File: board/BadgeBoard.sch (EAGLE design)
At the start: 63 parts

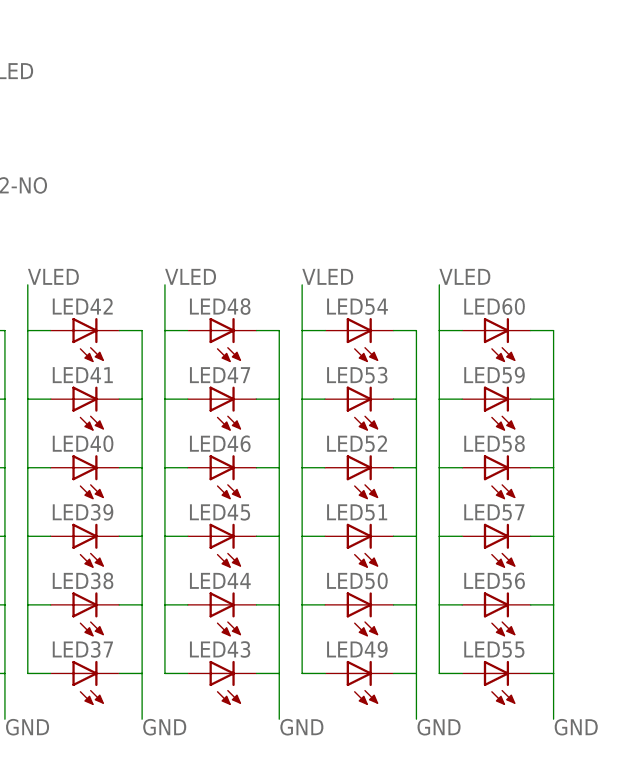
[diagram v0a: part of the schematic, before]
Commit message: add battery, redo layout a little
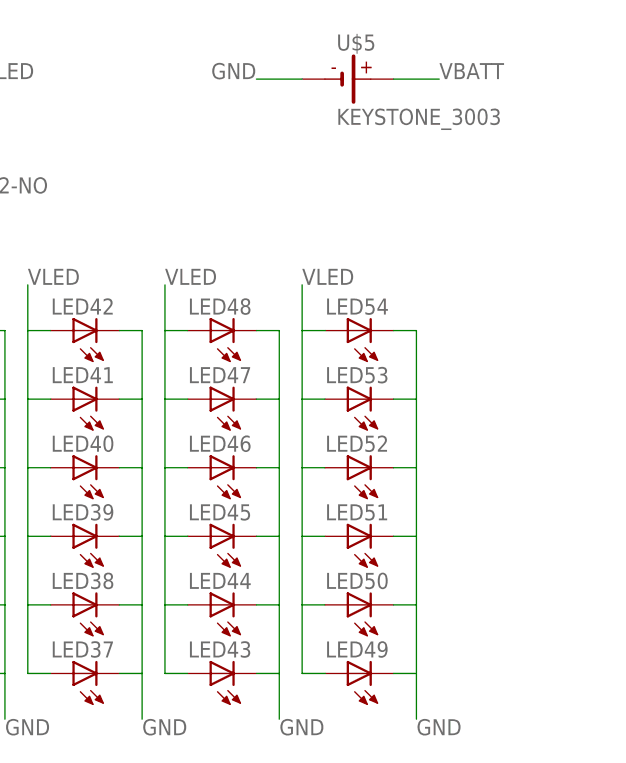
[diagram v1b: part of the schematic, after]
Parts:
- removed LED55, LED56, LED57, LED58, LED59, LED60: (no value), adafruit:LED3MM
- added U$5: KEYSTONE_3003, battery:KEYSTONE_3003
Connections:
- net GND: now also U$5.-; no longer LED55.C, LED56.C, LED57.C, LED58.C, LED59.C, LED60.C
- net VBATT: now also U$5.+
- net VLED: no longer LED55.A, LED56.A, LED57.A, LED58.A, LED59.A, LED60.A
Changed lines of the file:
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@@
 <part name="LED53" library="adafruit" deviceset="LED" device="3MM"/>
 <part name="LED54" library="adafruit" deviceset="LED" device="3MM"/>
-<part name="LED55" library="adafruit" deviceset="LED" device="3MM"/>
-<part name="LED56" library="adafruit" deviceset="LED" device="3MM"/>
-<part name="LED57" library="adafruit" deviceset="LED" device="3MM"/>
-<part name="LED58" library="adafruit" deviceset="LED" device="3MM"/>
-<part name="LED59" library="adafruit" deviceset="LED" device="3MM"/>
-<part name="LED60" library="adafruit" deviceset="LED" device="3MM"/>
 <part name="U$4" library="switch" deviceset="JS202011CQN" device=""/>
 <part name="R1" library="adafruit" deviceset="R-US_" device="0207/9"/>
 <part name="JP1" library="SparkFun-Passives" deviceset="JUMPER-PAD-2-NO" device=""/>
+<part name="U$5" library="battery" deviceset="KEYSTONE_3003" device=""/>
 </parts>
 <sheets>
@@
 <instance part="LED53" gate="G$1" x="129.54" y="35.56" rot="R90"/>
 <instance part="LED54" gate="G$1" x="129.54" y="43.18" rot="R90"/>
-<instance part="LED55" gate="G$1" x="144.78" y="5.08" rot="R90"/>
-<instance part="LED56" gate="G$1" x="144.78" y="12.7" rot="R90"/>
-<instance part="LED57" gate="G$1" x="144.78" y="20.32" rot="R90"/>
-<instance part="LED58" gate="G$1" x="144.78" y="27.94" rot="R90"/>
-<instance part="LED59" gate="G$1" x="144.78" y="35.56" rot="R90"/>
-<instance part="LED60" gate="G$1" x="144.78" y="43.18" rot="R90"/>
 <instance part="U$4" gate="G$1" x="30.48" y="71.12"/>
 <instance part="R1" gate="G$1" x="78.74" y="71.12"/>
 <instance part="JP1" gate="G$1" x="78.74" y="63.5"/>
+<instance part="U$5" gate="G$1" x="129.54" y="71.12"/>
 </instances>
 <busses>
@@
 </segment>
 <segment>
-<wire x1="139.7" y1="48.26" x2="139.7" y2="43.18" width="0.1524" layer="91"/>
-<wire x1="139.7" y1="43.18" x2="139.7" y2="35.56" width="0.1524" layer="91"/>
-<wire x1="139.7" y1="35.56" x2="139.7" y2="27.94" width="0.1524" layer="91"/>
-<wire x1="139.7" y1="27.94" x2="139.7" y2="20.32" width="0.1524" layer="91"/>
-<wire x1="139.7" y1="20.32" x2="139.7" y2="12.7" width="0.1524" layer="91"/>
-<wire x1="139.7" y1="12.7" x2="139.7" y2="5.08" width="0.1524" layer="91"/>
-<wire x1="139.7" y1="5.08" x2="142.24" y2="5.08" width="0.1524" layer="91"/>
-<label x="139.7" y="48.26" size="1.778" layer="95"/>
-<wire x1="139.7" y1="43.18" x2="142.24" y2="43.18" width="0.1524" layer="91"/>
-<wire x1="139.7" y1="35.56" x2="142.24" y2="35.56" width="0.1524" layer="91"/>
-<wire x1="139.7" y1="27.94" x2="142.24" y2="27.94" width="0.1524" layer="91"/>
-<wire x1="139.7" y1="20.32" x2="142.24" y2="20.32" width="0.1524" layer="91"/>
-<wire x1="139.7" y1="12.7" x2="142.24" y2="12.7" width="0.1524" layer="91"/>
-<pinref part="LED55" gate="G$1" pin="A"/>
-<pinref part="LED56" gate="G$1" pin="A"/>
-<pinref part="LED57" gate="G$1" pin="A"/>
-<pinref part="LED58" gate="G$1" pin="A"/>
-<pinref part="LED59" gate="G$1" pin="A"/>
-<pinref part="LED60" gate="G$1" pin="A"/>
-</segment>
-<segment>
 <wire x1="83.82" y1="71.12" x2="86.36" y2="71.12" width="0.1524" layer="91"/>
 <label x="88.9" y="71.12" size="1.778" layer="95"/>
@@
 </segment>
 <segment>
-<wire x1="149.86" y1="43.18" x2="152.4" y2="43.18" width="0.1524" layer="91"/>
-<wire x1="152.4" y1="43.18" x2="152.4" y2="35.56" width="0.1524" layer="91"/>
-<label x="152.4" y="0" size="1.778" layer="95" rot="MR180"/>
-<wire x1="152.4" y1="35.56" x2="152.4" y2="27.94" width="0.1524" layer="91"/>
-<wire x1="152.4" y1="27.94" x2="152.4" y2="20.32" width="0.1524" layer="91"/>
-<wire x1="152.4" y1="20.32" x2="152.4" y2="12.7" width="0.1524" layer="91"/>
-<wire x1="152.4" y1="12.7" x2="152.4" y2="5.08" width="0.1524" layer="91"/>
-<wire x1="152.4" y1="5.08" x2="152.4" y2="0" width="0.1524" layer="91"/>
-<wire x1="149.86" y1="35.56" x2="152.4" y2="35.56" width="0.1524" layer="91"/>
-<wire x1="149.86" y1="27.94" x2="152.4" y2="27.94" width="0.1524" layer="91"/>
-<wire x1="149.86" y1="5.08" x2="152.4" y2="5.08" width="0.1524" layer="91"/>
-<wire x1="149.86" y1="12.7" x2="152.4" y2="12.7" width="0.1524" layer="91"/>
-<wire x1="149.86" y1="20.32" x2="152.4" y2="20.32" width="0.1524" layer="91"/>
-<pinref part="LED55" gate="G$1" pin="C"/>
-<pinref part="LED56" gate="G$1" pin="C"/>
-<pinref part="LED57" gate="G$1" pin="C"/>
-<pinref part="LED58" gate="G$1" pin="C"/>
-<pinref part="LED59" gate="G$1" pin="C"/>
-<pinref part="LED60" gate="G$1" pin="C"/>
-</segment>
-<segment>
 <wire x1="134.62" y1="43.18" x2="137.16" y2="43.18" width="0.1524" layer="91"/>
 <wire x1="137.16" y1="43.18" x2="137.16" y2="35.56" width="0.1524" layer="91"/>
@@
 <pinref part="LED25" gate="G$1" pin="C"/>
 </segment>
+<segment>
+<pinref part="U$5" gate="G$1" pin="-"/>
+<wire x1="119.38" y1="71.12" x2="124.46" y2="71.12" width="0.1524" layer="91"/>
+<label x="119.38" y="71.12" size="1.778" layer="95" rot="MR0"/>
+</segment>
 </net>
 <net name="SW_BATT" class="0">
@@
 <label x="20.32" y="68.58" size="1.778" layer="95" rot="MR0"/>
 </segment>
+<segment>
+<pinref part="U$5" gate="G$1" pin="+"/>
+<wire x1="134.62" y1="71.12" x2="139.7" y2="71.12" width="0.1524" layer="91"/>
+<label x="139.7" y="71.12" size="1.778" layer="95"/>
+</segment>
 </net>
